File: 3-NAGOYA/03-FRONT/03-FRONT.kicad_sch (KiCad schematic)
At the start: 34 parts, among them J2 PC-PD, J2 WRITER CONN, J4 PA0-7, J5 PB3-9, J6 OpenMV Conn, J6 PB0-2, J7 PB14-15, J8 PB12, J9 PA8, U1 STM32F103C8Tx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

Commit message: 03-FRONT部品割り当て終わり
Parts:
- J4: footprint (none) -> Connector_PinHeader_2.54mm:PinHeader_1x08_P2.54mm_Vertical
- J5: footprint (none) -> Connector_PinHeader_2.54mm:PinHeader_1x07_P2.54mm_Vertical
- J6: footprint (none) -> Connector_PinHeader_2.54mm:PinHeader_1x03_P2.54mm_Vertical
- J7: footprint (none) -> Connector_PinHeader_2.54mm:PinHeader_1x02_P2.54mm_Vertical
- J8, J9: footprint (none) -> Connector_PinHeader_2.54mm:PinHeader_1x01_P2.54mm_Vertical
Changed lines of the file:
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@@
       (effects (font (size 1.27 1.27)))
     )
-    (property "Footprint" "" (at 203.835 99.695 0)
+    (property "Footprint" "Connector_PinHeader_2.54mm:PinHeader_1x01_P2.54mm_Vertical" (at 203.835 99.695 0)
       (effects (font (size 1.27 1.27)) hide)
     )
@@
       (effects (font (size 1.27 1.27)) (justify left))
     )
-    (property "Footprint" "" (at 247.015 48.895 0)
+    (property "Footprint" "Connector_PinHeader_2.54mm:PinHeader_1x08_P2.54mm_Vertical" (at 247.015 48.895 0)
       (effects (font (size 1.27 1.27)) hide)
     )
@@
       (effects (font (size 1.27 1.27)))
     )
-    (property "Footprint" "" (at 247.015 61.595 0)
+    (property "Footprint" "Connector_PinHeader_2.54mm:PinHeader_1x01_P2.54mm_Vertical" (at 247.015 61.595 0)
       (effects (font (size 1.27 1.27)) hide)
     )
@@
       (effects (font (size 1.27 1.27)))
     )
-    (property "Footprint" "" (at 203.835 84.455 0)
+    (property "Footprint" "Connector_PinHeader_2.54mm:PinHeader_1x07_P2.54mm_Vertical" (at 203.835 84.455 0)
       (effects (font (size 1.27 1.27)) hide)
     )
@@
       (effects (font (size 1.27 1.27)))
     )
-    (property "Footprint" "" (at 203.835 71.755 0)
+    (property "Footprint" "Connector_PinHeader_2.54mm:PinHeader_1x03_P2.54mm_Vertical" (at 203.835 71.755 0)
       (effects (font (size 1.27 1.27)) hide)
     )
@@
       (effects (font (size 1.27 1.27)))
     )
-    (property "Footprint" "" (at 203.835 107.315 0)
-      (effects (font (size 1.27 1.27)) hide)
-    )
+    (property "Footprint" "Connector_PinHeader_2.54mm:PinHeader_1x02_P2.54mm_Vertical" (at 203.835 107.315 0)
+      (effects (font (size 1.27 1.27)) hide)
+    )

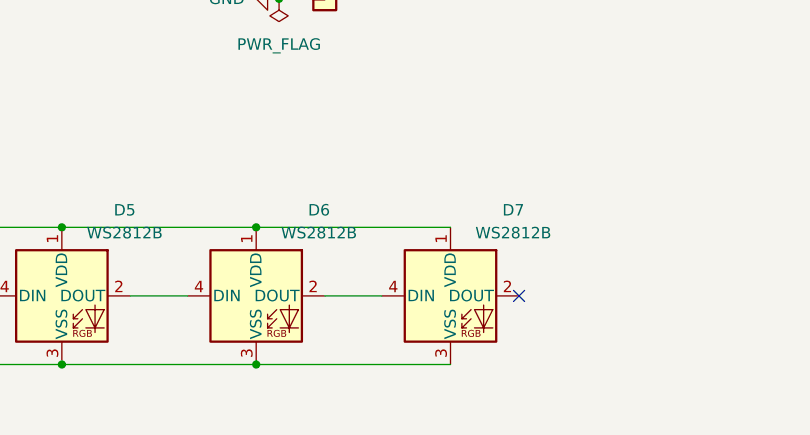
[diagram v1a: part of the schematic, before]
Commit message: 03-FRONT部品配置終わり
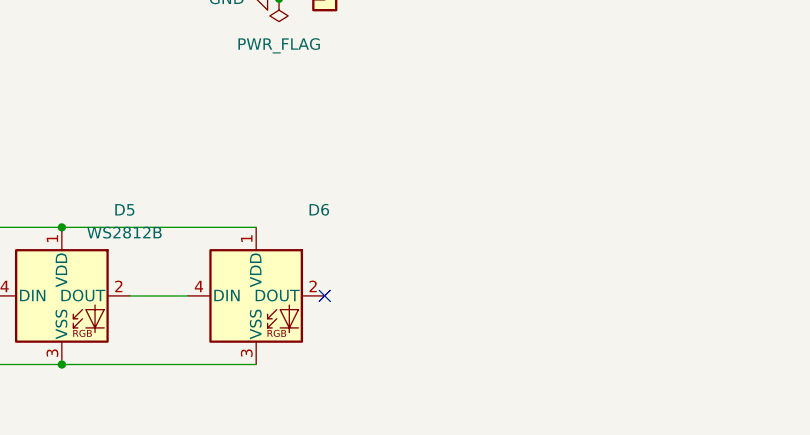
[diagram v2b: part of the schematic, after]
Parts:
- removed D7: WS2812B, LED_SMD:LED_WS2812B_PLCC4_5.0x5.0mm_P3.2mm, symbol LED:WS2812B
- J2: footprint Connector_PinSocket_2.54mm:PinSocket_2x04_P2.54mm_Horizontal -> Connector_PinSocket_2.54mm:PinSocket_2x04_P2.54mm_Vertical
- J6: footprint Connector_JST:JST_XH_S4B-XH-A_1x04_P2.50mm_Horizontal -> Connector_JST:JST_XH_B4B-XH-A_1x04_P2.50mm_Vertical
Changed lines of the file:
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@@
 (kicad_sch (version 20230121) (generator eeschema)
   (paper "A4")
-  (junction (at 132.715 181.61) (diameter 0) (color 0 0 0 0)
-  )
   (junction (at 111.125 166.37) (diameter 0) (color 0 0 0 0)
   )
@@
   )
   (junction (at 135.255 140.97) (diameter 0) (color 0 0 0 0)
-  )
-  (junction (at 132.715 166.37) (diameter 0) (color 0 0 0 0)
   )
   (junction (at 47.625 166.37) (diameter 0) (color 0 0 0 0)
@@
   (no_connect (at 129.54 110.49))
   (no_connect (at 95.885 48.26))
-  (no_connect (at 161.925 173.99))
   (no_connect (at 50.8 102.87))
   (no_connect (at 95.885 76.835))
+  (no_connect (at 140.335 173.99))
   (wire (pts (xy 76.835 173.99) (xy 83.185 173.99))
     (stroke (width 0) (type default))
@@
     (stroke (width 0) (type default))
   )
-  (wire (pts (xy 140.335 173.99) (xy 146.685 173.99))
-    (stroke (width 0) (type default))
-  )
   (wire (pts (xy 202.565 34.29) (xy 213.995 34.29))
     (stroke (width 0) (type default))
@@
     (stroke (width 0) (type default))
   )
-  (wire (pts (xy 132.715 181.61) (xy 154.305 181.61))
-    (stroke (width 0) (type default))
-  )
   (wire (pts (xy 180.34 34.29) (xy 191.77 34.29))
     (stroke (width 0) (type default))
@@
   )
   (wire (pts (xy 191.77 34.29) (xy 202.565 34.29))
-    (stroke (width 0) (type default))
-  )
-  (wire (pts (xy 132.715 166.37) (xy 154.305 166.37))
     (stroke (width 0) (type default))
   )
@@
     )
     (property "Value" "WS2812B" (at 139.7 167.005 0)
-      (effects (font (size 1.27 1.27)))
+      (effects (font (size 1.27 1.27)) hide)
     )
     (property "Footprint" "LED_SMD:LED_WS2812B_PLCC4_5.0x5.0mm_P3.2mm" (at 133.985 181.61 0)
@@
     )
   )
-  (symbol (lib_id "LED:WS2812B") (at 154.305 173.99 0) (unit 1)
-    (in_bom yes) (on_board yes) (dnp no)
-    (property "Reference" "D7" (at 161.29 164.465 0)
-      (effects (font (size 1.27 1.27)))
-    )
-    (property "Value" "WS2812B" (at 161.29 167.005 0)
-      (effects (font (size 1.27 1.27)))
-    )
-    (property "Footprint" "LED_SMD:LED_WS2812B_PLCC4_5.0x5.0mm_P3.2mm" (at 155.575 181.61 0)
-      (effects (font (size 1.27 1.27)) (justify left top) hide)
-    )
-    (property "Datasheet" "https://cdn-shop.adafruit.com/datasheets/WS2812B.pdf" (at 156.845 183.515 0)
-      (effects (font (size 1.27 1.27)) (justify left top) hide)
-    )
-    (pin "3")
-    (pin "4")
-    (pin "1")
-    (pin "2")
-    (instances
-      (project "03-FRONT"
-        (path "/e118ed56-ce79-44d8-8eff-a935fd9f7b40"
-          (reference "D7") (unit 1)
-        )
-      )
-    )
-  )
   (symbol (lib_id "LED:WS2812B") (at 90.805 173.99 0) (unit 1)
     (in_bom yes) (on_board yes) (dnp no)
@@
       (effects (font (size 1.27 1.27)))
     )
-    (property "Footprint" "Connector_PinSocket_2.54mm:PinSocket_2x04_P2.54mm_Horizontal" (at 134.62 113.03 0)
+    (property "Footprint" "Connector_PinSocket_2.54mm:PinSocket_2x04_P2.54mm_Vertical" (at 134.62 113.03 0)
       (effects (font (size 1.27 1.27)) hide)
     )
@@
       (effects (font (size 1.27 1.27)) (justify left))
     )
-    (property "Footprint" "Connector_JST:JST_XH_S4B-XH-A_1x04_P2.50mm_Horizontal" (at 140.335 135.89 0)
-      (effects (font (size 1.27 1.27)) hide)
-    )
+    (property "Footprint" "Connector_JST:JST_XH_B4B-XH-A_1x04_P2.50mm_Vertical" (at 140.335 135.89 0)
+      (effects (font (size 1.27 1.27)) hide)
+    )

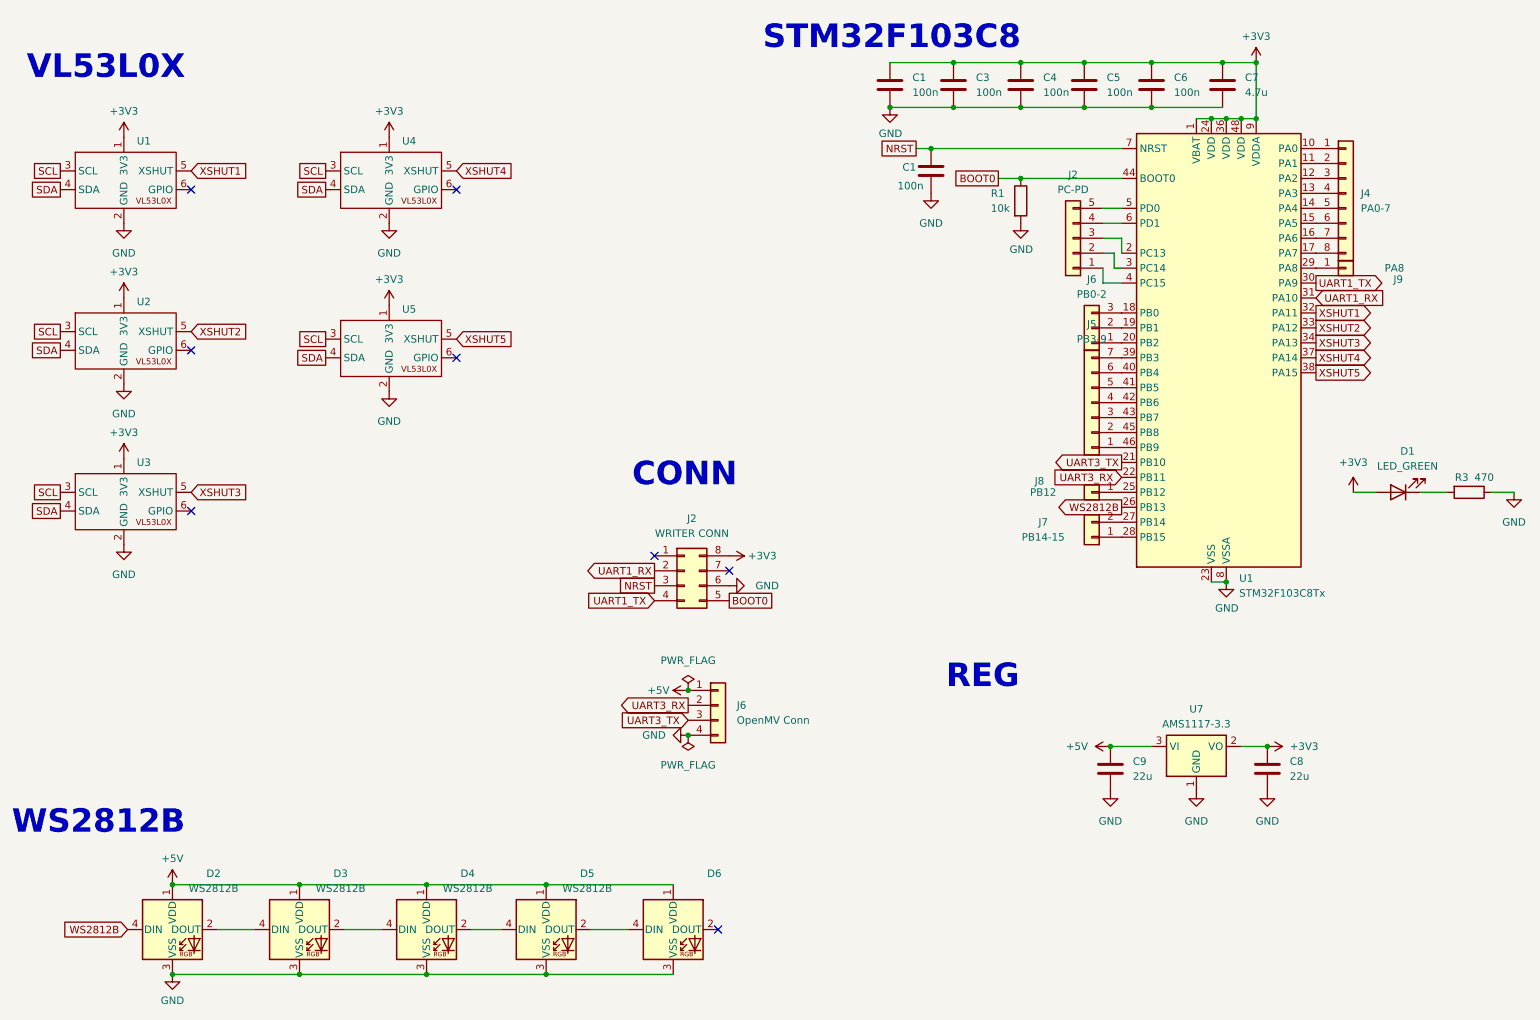
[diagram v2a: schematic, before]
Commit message: 03-FRONT XIAOに変更
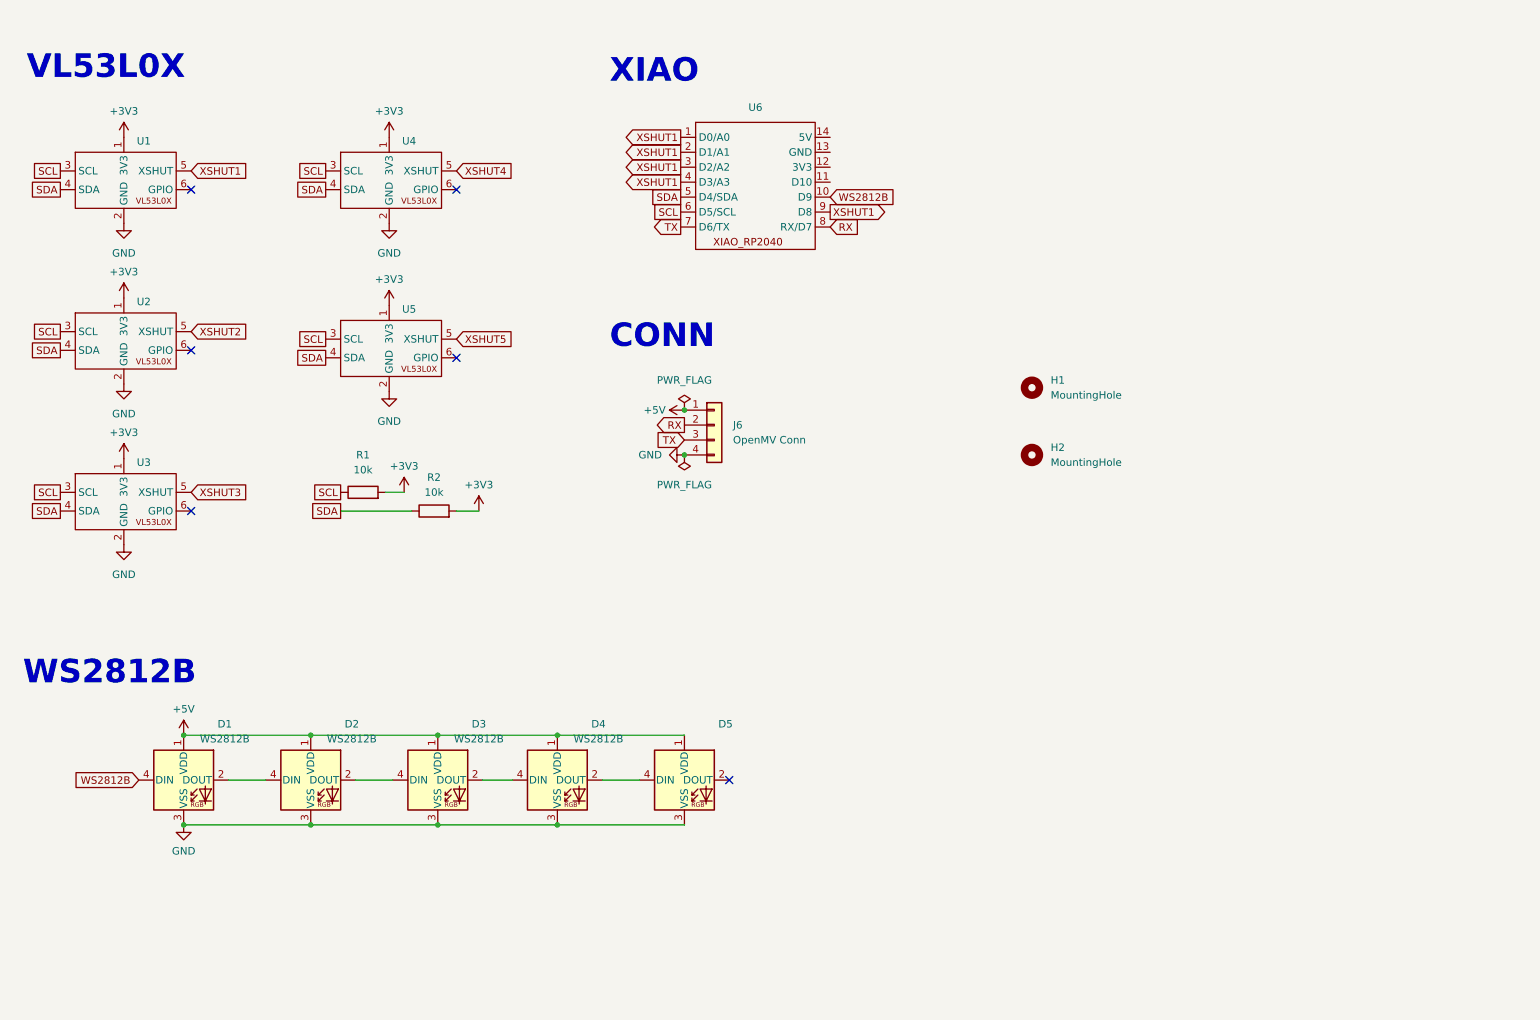
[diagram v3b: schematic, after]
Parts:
- removed C1 (x2), C3, C4, C5, C6: 100n, Capacitor_SMD:C_0402_1005Metric, symbol Device:C
- removed C7: 4.7u, Resistor_SMD:R_0402_1005Metric, symbol Device:C
- removed C8, C9: 22u, Capacitor_SMD:C_0805_2012Metric, symbol Device:C
- removed D1: LED_GREEN, LED_SMD:LED_0805_2012Metric, symbol Device:LED
- removed J2: WRITER CONN, Connector_PinSocket_2.54mm:PinSocket_2x04_P2.54mm_Vertical, symbol Connector_Generic:Conn_02x04_Counter_Clockwise
- removed J2: PC-PD, Connector_PinHeader_2.54mm:PinHeader_1x05_P2.54mm_Vertical, symbol Connector_Generic:Conn_01x05
- removed J4: PA0-7, Connector_PinHeader_2.54mm:PinHeader_1x08_P2.54mm_Vertical, symbol Connector_Generic:Conn_01x08
- removed J5: PB3-9, Connector_PinHeader_2.54mm:PinHeader_1x07_P2.54mm_Vertical, symbol Connector_Generic:Conn_01x07
- removed J6: PB0-2, Connector_PinHeader_2.54mm:PinHeader_1x03_P2.54mm_Vertical, symbol Connector_Generic:Conn_01x03
- removed J7: PB14-15, Connector_PinHeader_2.54mm:PinHeader_1x02_P2.54mm_Vertical, symbol Connector_Generic:Conn_01x02
- removed J8: PB12, Connector_PinHeader_2.54mm:PinHeader_1x01_P2.54mm_Vertical, symbol Connector_Generic:Conn_01x01
- removed J9: PA8, Connector_PinHeader_2.54mm:PinHeader_1x01_P2.54mm_Vertical, symbol Connector_Generic:Conn_01x01
- removed R3: 470, Resistor_SMD:R_0603_1608Metric, symbol Device:R
- removed U1: STM32F103C8Tx, Package_QFP:LQFP-48_7x7mm_P0.5mm, symbol MCU_ST_STM32F1:STM32F103C8Tx
- removed U7: AMS1117-3.3, Package_TO_SOT_SMD:SOT-223-3_TabPin2, symbol Regulator_Linear:AMS1117-3.3
- added H1, H2: MountingHole, MountingHole:MountingHole_3.2mm_M3, symbol Mechanical:MountingHole
- added R2: 10k, Resistor_THT:R_Axial_DIN0207_L6.3mm_D2.5mm_P10.16mm_Horizontal, symbol Device:R
- added U6: ~, XIAO:MOUDLE14P-2.54-21X17.8MM, symbol XIAO:XIAO_RP2040
- R1: footprint Resistor_SMD:R_0603_1608Metric -> Resistor_THT:R_Axial_DIN0207_L6.3mm_D2.5mm_P10.16mm_Horizontal; LCSC C25804 -> (none)
- renumbered D2 to D1, D3 to D2, D4 to D3, D5 to D4, D6 to D5
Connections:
- net BOOT0 is gone; now on net SCL: R1.1
- net +3V3: now also R1.2, R2.2
- net GND: no longer R1.2
- net SCL: now also U6.6 (D5/SCL)
- net SDA: now also R2.1, U6.5 (D4/SDA)
- net WS2812B: now also U6.10 (D9)
- net XSHUT1: now also U6.1 (D0/A0), U6.2 (D1/A1), U6.3 (D2/A2), U6.4 (D3/A3), U6.9 (D8)
- net UART3_RX renamed RX
- net RX: now also U6.8 (RX/D7)
- net UART3_TX renamed TX
- net TX: now also U6.7 (D6/TX)
- no-connect marks 8 -> 6
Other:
- note added: "XIAO"
- note removed: "REG"
- note removed: "STM32F103C8"
- moved on the sheet: D1, D2, D3, D4, D5, J6

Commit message: 06-UI完成
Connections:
- net +3V3: now also U6.12 (3V3)
- net +5V: now also U6.14 (5V)
- net GND: now also U6.13 (GND)
- net XSHUT1: no longer U6.2 (D1/A1), U6.3 (D2/A2), U6.4 (D3/A3), U6.9 (D8)
- net XSHUT2: now also U6.2 (D1/A1)
- net XSHUT3: now also U6.3 (D2/A2)
- net XSHUT4: now also U6.4 (D3/A3)
- net XSHUT5: now also U6.9 (D8)
- no-connect marks 6 -> 7
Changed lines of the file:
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@@
   (no_connect (at 50.8 48.26))
   (no_connect (at 50.8 75.565))
+  (no_connect (at 159.385 46.99))
   (no_connect (at 95.885 48.26))
   (no_connect (at 50.8 102.87))
@@
     (stroke (width 0) (type default))
   )
+  (wire (pts (xy 168.91 44.45) (xy 159.385 44.45))
+    (stroke (width 0) (type default))
+  )
   (wire (pts (xy 49.53 156.21) (xy 71.12 156.21))
     (stroke (width 0) (type default))
@@
   )
   (wire (pts (xy 86.995 99.695) (xy 83.82 99.695))
+    (stroke (width 0) (type default))
+  )
+  (wire (pts (xy 165.1 39.37) (xy 159.385 39.37))
     (stroke (width 0) (type default))
   )
@@
     )
   )
-  (global_label "XSHUT1" (shape output) (at 133.985 41.91 180) (fields_autoplaced)
+  (global_label "XSHUT2" (shape output) (at 133.985 41.91 180) (fields_autoplaced)
     (effects (font (size 1.27 1.27)) (justify right))
     (property "Intersheetrefs" "${INTERSHEET_REFS}" (at 123.7427 41.91 0)
@@
     )
   )
-  (global_label "XSHUT1" (shape output) (at 159.385 52.07 0) (fields_autoplaced)
+  (global_label "XSHUT5" (shape output) (at 159.385 52.07 0) (fields_autoplaced)
     (effects (font (size 1.27 1.27)) (justify left))
     (property "Intersheetrefs" "${INTERSHEET_REFS}" (at 169.6273 52.07 0)
@@
     )
   )
-  (global_label "XSHUT1" (shape output) (at 133.985 44.45 180) (fields_autoplaced)
+  (global_label "XSHUT3" (shape output) (at 133.985 44.45 180) (fields_autoplaced)
     (effects (font (size 1.27 1.27)) (justify right))
     (property "Intersheetrefs" "${INTERSHEET_REFS}" (at 123.7427 44.45 0)
@@
     )
   )
-  (global_label "XSHUT1" (shape output) (at 133.985 46.99 180) (fields_autoplaced)
+  (global_label "XSHUT4" (shape output) (at 133.985 46.99 180) (fields_autoplaced)
     (effects (font (size 1.27 1.27)) (justify right))
     (property "Intersheetrefs" "${INTERSHEET_REFS}" (at 123.7427 46.99 0)
@@
         (path "/e118ed56-ce79-44d8-8eff-a935fd9f7b40"
           (reference "D2") (unit 1)
+        )
+      )
+    )
+  )
+  (symbol (lib_id "power:+3V3") (at 168.91 44.45 0) (unit 1)
+    (in_bom yes) (on_board yes) (dnp no) (fields_autoplaced)
+    (property "Reference" "#PWR018" (at 168.91 48.26 0)
+      (effects (font (size 1.27 1.27)) hide)
+    )
+    (property "Value" "+3V3" (at 168.91 39.37 0)
+      (effects (font (size 1.27 1.27)))
+    )
+    (property "Footprint" "" (at 168.91 44.45 0)
+      (effects (font (size 1.27 1.27)) hide)
+    )
+    (property "Datasheet" "" (at 168.91 44.45 0)
+      (effects (font (size 1.27 1.27)) hide)
+    )
+    (pin "1")
+    (instances
+      (project "03-FRONT"
+        (path "/e118ed56-ce79-44d8-8eff-a935fd9f7b40"
+          (reference "#PWR018") (unit 1)
+        )
+      )
+    )
+  )
+  (symbol (lib_id "power:GND") (at 159.385 41.91 90) (unit 1)
+    (in_bom yes) (on_board yes) (dnp no) (fields_autoplaced)
+    (property "Reference" "#PWR019" (at 165.735 41.91 0)
+      (effects (font (size 1.27 1.27)) hide)
+    )
+    (property "Value" "GND" (at 162.56 41.91 90)
+      (effects (font (size 1.27 1.27)) (justify right))
+    )
+    (property "Footprint" "" (at 159.385 41.91 0)
+      (effects (font (size 1.27 1.27)) hide)
+    )
+    (property "Datasheet" "" (at 159.385 41.91 0)
+      (effects (font (size 1.27 1.27)) hide)
+    )
+    (pin "1")
+    (instances
+      (project "03-FRONT"
+        (path "/e118ed56-ce79-44d8-8eff-a935fd9f7b40"
+          (reference "#PWR019") (unit 1)
         )
       )
@@
         )
       )
+    )
+  )
+  (symbol (lib_id "power:+5V") (at 165.1 39.37 0) (unit 1)
+    (in_bom yes) (on_board yes) (dnp no) (fields_autoplaced)
+    (property "Reference" "#PWR017" (at 165.1 43.18 0)
+      (effects (font (size 1.27 1.27)) hide)
+    )
+    (property "Value" "+5V" (at 165.1 34.29 0)
+      (effects (font (size 1.27 1.27)))
+    )
+    (property "Footprint" "" (at 165.1 39.37 0)
+      (effects (font (size 1.27 1.27)) hide)
+    )
+    (property "Datasheet" "" (at 165.1 39.37 0)
+      (effects (font (size 1.27 1.27)) hide)
+    )
+    (pin "1")
+    (instances
+      (project "03-FRONT"
+        (path "/e118ed56-ce79-44d8-8eff-a935fd9f7b40"
+          (reference "#PWR017") (unit 1)
+        )
+      )
